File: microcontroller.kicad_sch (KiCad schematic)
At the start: 65 parts, among them J4 Conn_01x03_Pin, J5 Conn_01x05_Pin, J6 Conn_02x04_Odd_Even, J7 Conn_02x15_Counter_Clockwise, SW2 SW_Push, SW3 SW_Push, U3 RP2040, U5 W25Q16JVSS, U6 W25Q16JVSS, Y1 12MHz/10pF, Y2 12MHz/10pF

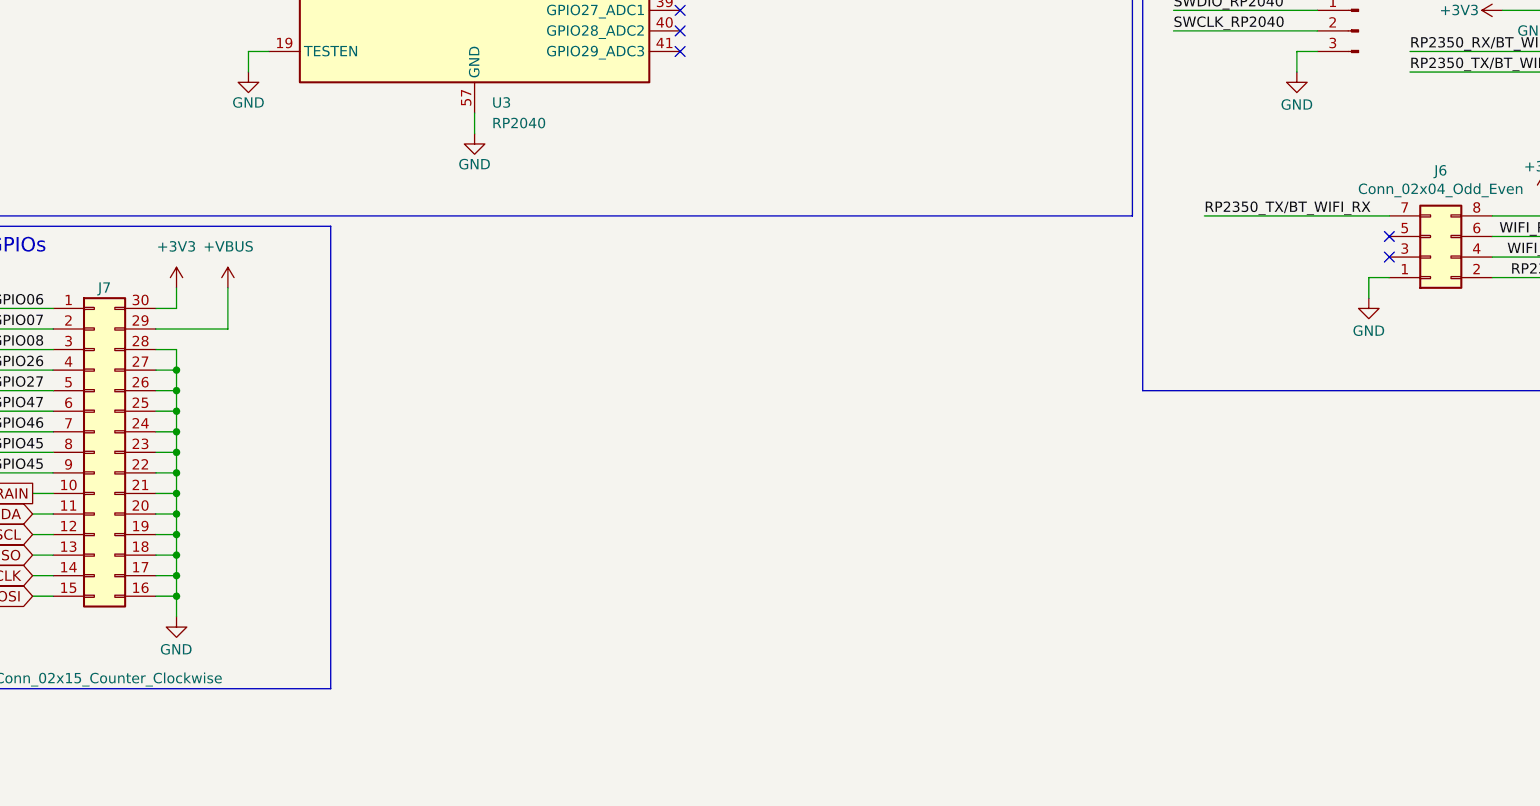
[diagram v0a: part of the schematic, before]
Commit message: feat: adds pull-up resistors to wi-fi header
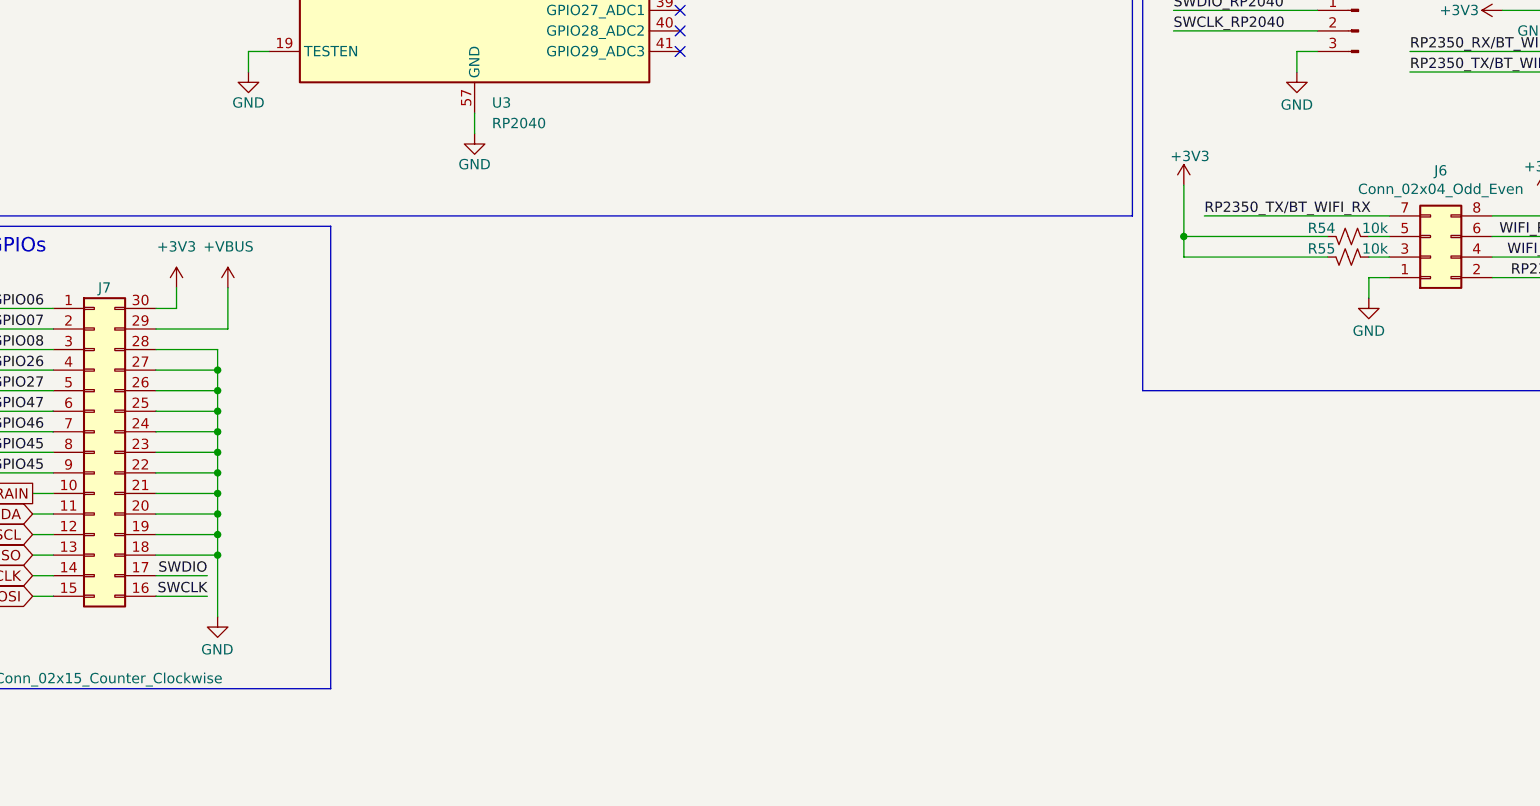
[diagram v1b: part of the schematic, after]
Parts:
- added R54, R55: 10k, Resistor_SMD:R_0402_1005Metric, symbol Device:R_Small_US
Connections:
- net +3V3: now also R54.2, R55.2
- net GND: no longer J7.16 (Pin_16), J7.17 (Pin_17)
- net SWCLK: now also J7.16 (Pin_16)
- net SWDIO: now also J7.17 (Pin_17)
- net at J6.3 (Pin_3): now also R55.1
- net at J6.5 (Pin_5): now also R54.1
- no-connect marks 28 -> 26

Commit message: chore: updates display capacitors
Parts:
- C22, C8, C9: MPN CL05A475MP5NRNC -> CL05A105KA5NQNC
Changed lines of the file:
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@@
 			)
 		)
-		(property "Datasheet" "https://www.digikey.com.br/en/products/detail/samsung-electro-mechanics/CL05A475MP5NRNC/3887140"
+		(property "Datasheet" "https://www.digikey.com.br/en/products/detail/samsung-electro-mechanics/CL05A105KA5NQNC/3889531"
 			(at 128.27 46.99 0)
 			(effects
@@
 			)
 		)
-		(property "MPN" "CL05A475MP5NRNC"
+		(property "MPN" "CL05A105KA5NQNC"
 			(at 128.27 46.99 0)
 			(effects
@@
 			)
 		)
-		(property "Datasheet" "https://www.digikey.com.br/en/products/detail/samsung-electro-mechanics/CL05A475MP5NRNC/3887140"
+		(property "Datasheet" "https://www.digikey.com.br/en/products/detail/samsung-electro-mechanics/CL05A105KA5NQNC/3889531"
 			(at 118.11 46.99 0)
 			(effects
@@
 			)
 		)
-		(property "MPN" "CL05A475MP5NRNC"
+		(property "MPN" "CL05A105KA5NQNC"
 			(at 118.11 46.99 0)
 			(effects
@@
 			)
 		)
-		(property "Datasheet" "https://www.digikey.com.br/en/products/detail/samsung-electro-mechanics/CL05A475MP5NRNC/3887140"
+		(property "Datasheet" "https://www.digikey.com.br/en/products/detail/samsung-electro-mechanics/CL05A105KA5NQNC/3889531"
 			(at 134.62 73.66 0)
 			(effects
@@
 			)
 		)
-		(property "MPN" "CL05A475MP5NRNC"
+		(property "MPN" "CL05A105KA5NQNC"
 			(at 134.62 73.66 0)
 			(effects

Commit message: wip: placement
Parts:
- removed J4: Conn_01x03_Pin, Connector_PinHeader_2.54mm:PinHeader_1x03_P2.54mm_Vertical, symbol Connector:Conn_01x03_Pin
- added J4: Conn_01x05_Pin, microcontroller:PogoPins, symbol Connector:Conn_01x05_Pin
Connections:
- net RP2350_RX/BT_WIFI_TX is gone; now on net RP2350_RX/BT_TX: J5.2 (Pin_2), J6.2 (Pin_2)
- net RP2350_TX/BT_WIFI_RX is gone; now on net RP2350_TX/BT_RX: J5.1 (Pin_1), J6.7 (Pin_7)
- net +3V3: now also J4.1 (Pin_1)
- net GND: now also J4.5 (Pin_5)
- net GPIO07: now also J7.1 (Pin_1); no longer J7.2 (Pin_2)
- net GPIO08: now also J7.2 (Pin_2); no longer J7.3 (Pin_3)
- net GPIO26: now also J7.3 (Pin_3); no longer J7.4 (Pin_4)
- net GPIO27: now also J7.4 (Pin_4); no longer J7.5 (Pin_5)
- net GPIO45: now also J7.7 (Pin_7); no longer J7.9 (Pin_9)
- net GPIO46: now also J7.6 (Pin_6); no longer J7.7 (Pin_7)
- net GPIO47: now also J7.5 (Pin_5); no longer J7.6 (Pin_6)
- net I2C_SCL: now also J7.11 (Pin_11); no longer J7.12 (Pin_12)
- net I2C_SDA: now also J7.10 (Pin_10); no longer J7.11 (Pin_11)
- net MOSFET_DRAIN: now also J7.9 (Pin_9); no longer J7.10 (Pin_10)
- net RUN_RP2040: now also J4.4 (Pin_4)
- net RUN_RP2350: now also J7.15 (Pin_15)
- net SPI_MISO: now also J7.12 (Pin_12); no longer J7.13 (Pin_13)
- net SPI_MOSI: now also J7.14 (Pin_14); no longer J7.15 (Pin_15)
- net SPI_SCLK: now also J7.13 (Pin_13); no longer J7.14 (Pin_14)
- net SWCLK_RP2040: now also J4.2 (Pin_2)
- net SWDIO_RP2040: now also J4.3 (Pin_3)
- net DISPLAY_RST renamed ~{DISPLAY_RST}
- net GPIO06 renamed LED_ADDR_GPIO
- net LED_ADDR_GPIO: no longer J7.1 (Pin_1)

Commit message: feat: starts routing
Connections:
- net +1V1: no longer C10.1, C18.1, C20.2, U3.23 (DVDD), U3.45 (VREG_VOUT), U3.50 (DVDD)
- new net +1V1_PROBE: C10.1, C18.1, C20.2, U3.23 (DVDD), U3.45 (VREG_VOUT), U3.50 (DVDD)
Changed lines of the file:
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@@
 			)
 		)
-		(property "Value" "+1V1"
+		(property "Value" "+1V1_PROBE"
 			(at 243.84 40.64 0)
 			(effects

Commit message: wip: adds more routing
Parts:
- removed C25: 100n, Capacitor_SMD:C_0402_1005Metric, symbol Device:C_Small
- removed R22: 1k, Resistor_SMD:R_0402_1005Metric, symbol Device:R_Small_US
- removed SW3: SW_Push, Button_Switch_THT:SW_PUSH_6mm_H4.3mm, symbol Switch:SW_Push
- renumbered C13 to C10, C14 to C11, C15 to C12, C16 to C13, C17 to C14, C18 to C15, C19 to C16, C20 to C17, C21 to C18, C22 to C19, C23 to C20, C24 to C21, C26 to C22, C27 to C23, C28 to C24, C29 to C25, C30 to C26, C31 to C27, C32 to C28, C33 to C29, C6 to C3, C34 to C30, C35 to C31, C36 to C32, C37 to C33, C38 to C34, C39 to C35, C40 to C36, C7 to C4, C8 to C5, C9 to C6, C10 to C7, C11 to C8, C12 to C9, D8 to D5, J4 to J3, J5 to J4, J6 to J5, J7 to J6, R19 to R10, R20 to R11, R21 to R12, R24 to R13, R23 to R14, R54 to R15, R55 to R16, R53 to R17, R25 to R18, R26 to R19, R16 to R7, R17 to R8, R18 to R9, SW2 to SW1, TP11 to TP10, TP8 to TP7, TP9 to TP8, TP10 to TP9, U3 to U2, U4 to U3, U5 to U4, U6 to U5
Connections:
- net BUTTON2_GPIO: now also U3.25 (GPIO24); no longer U3.23 (GPIO23)
- net BUTTON3_GPIO: now also U3.26 (GPIO25); no longer U3.25 (GPIO24)
- net BUTTON4_GPIO: now also U3.23 (GPIO23); no longer U3.26 (GPIO25)
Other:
- note added: "RESET Button"
- note removed: "RESET Buttons"
- moved on the sheet: D5, J3, J4, J5, R13, R15, R16

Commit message: feat: finishes p1 routing
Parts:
- added TP19, TP20, TP21: TestPoint_Small, TestPoint:TestPoint_Pad_D1.0mm, symbol Connector:TestPoint_Small
- D5, J4, R13: now not fitted
- J6: symbol Connector_Generic:Conn_02x15_Counter_Clockwise -> Connector_Generic:Conn_02x15_Odd_Even
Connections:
- net +3V3: now also J6.1 (Pin_1); no longer J6.30 (Pin_30)
- net +VBUS: now also J6.2 (Pin_2); no longer J6.29 (Pin_29)
- net GND: now also J6.11 (Pin_11), J6.13 (Pin_13), J6.15 (Pin_15), J6.17 (Pin_17), J6.29 (Pin_29), J6.3 (Pin_3), J6.5 (Pin_5), J6.7 (Pin_7), J6.9 (Pin_9); no longer J6.18 (Pin_18), J6.20 (Pin_20), J6.22 (Pin_22), J6.24 (Pin_24), J6.25 (Pin_25), J6.26 (Pin_26), J6.28 (Pin_28)
- net GPIO07: now also J6.10 (Pin_10); no longer J6.1 (Pin_1)
- net GPIO08: now also J6.8 (Pin_8); no longer J6.2 (Pin_2)
- net GPIO26: now also J6.26 (Pin_26); no longer J6.3 (Pin_3)
- net GPIO27: now also J6.25 (Pin_25); no longer J6.4 (Pin_4)
- net GPIO45: now also J6.18 (Pin_18); no longer J6.7 (Pin_7), J6.8 (Pin_8), U3.55 (GPIO44_ADC4)
- net GPIO46: now also J6.16 (Pin_16); no longer J6.6 (Pin_6)
- net GPIO47: now also J6.14 (Pin_14); no longer J6.5 (Pin_5)
- net I2C_SCL: now also J6.4 (Pin_4); no longer J6.11 (Pin_11)
- net I2C_SDA: now also J6.6 (Pin_6); no longer J6.10 (Pin_10)
- net MOSFET_DRAIN: now also J6.22 (Pin_22); no longer J6.9 (Pin_9)
- net RUN_RP2350: now also TP21.1; no longer J6.15 (Pin_15)
- net SPI_MISO: now also J6.24 (Pin_24); no longer J6.12 (Pin_12)
- net SPI_MOSI: now also J6.30 (Pin_30); no longer J6.14 (Pin_14)
- net SPI_SCLK: now also J6.28 (Pin_28); no longer J6.13 (Pin_13)
- net SWCLK: now also TP19.1; no longer J6.16 (Pin_16)
- net SWDIO: now also TP20.1; no longer J6.17 (Pin_17)
- net POTENTIOMETER2_ADC renamed GPIO43
- net GPIO43: now also J6.12 (Pin_12)
- new net GPIO44: J6.20 (Pin_20), U3.55 (GPIO44_ADC4)
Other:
- moved on the sheet: C30

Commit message: chore: updates some parameters in components
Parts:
- J5: MPN (none) -> 61300821821

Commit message: fix: fixes schematic errors and some layout errors
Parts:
- C19, C5, C6: MPN CL05A105KA5NQNC -> CL05A475MP5NRNC
- J6: MPN (none) -> PPPC152LFBN-RC
- L1: footprint Inductor_SMD:L_0805_2012Metric_Pad1.05x1.20mm_HandSolder -> Inductor_SMD:L_0805_2012Metric_Pad1.15x1.40mm_HandSolder
- SW1: footprint Button_Switch_THT:SW_PUSH_6mm_H4.3mm -> peripherals1:SW_1825910-6-4; symbol Switch:SW_Push -> peripherals1:switch_button
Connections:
- net RUN_RP2350: now also SW1.3; no longer SW1.2
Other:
- moved on the sheet: TP10, TP21, TP9
